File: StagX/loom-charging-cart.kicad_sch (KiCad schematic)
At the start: 0 parts

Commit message: Post comp commit
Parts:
- added BT1: ACCU, symbol Device:Battery
- added Conn: AMPHENOL-21P-Recepticle, symbol Connectors_SUFST:AMPHENOL-21P-Recepticle
- added Conn1, Conn4: Molex_2x1P_Horizontal_THT, symbol Connectors_SUFST:Molex_2x1P_Horizontal_THT
- added Conn5, Conn6: Molex_2x2P_Horizontal, symbol Connectors_SUFST:Molex_2x2P_Horizontal
- added Conn7: AMPHENOL-47P-Recepticle, symbol Connectors_SUFST:AMPHENOL-47P-Recepticle
- added D1: IMD Fault, symbol Device:LED
- added D2: BMS Fault, symbol Device:LED
- added J1: MAINS 16A, symbol Connector_Generic:Conn_01x03
- added J2: CAN_S, symbol Connector:Conn_01x09_Pin
- added K1: Relay_DPST-NO, symbol Relay:Relay_DPST-NO
- added SW1: E-Stop, symbol Switch:SW_Push_Open
- added SW2: Latching Reset, symbol Switch:SW_Push
- added SW3: Close AIRs, symbol Switch:SW_SPST
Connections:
- new net: J1.2 (Pin_2), K1.13
- new net: J1.1 (Pin_1), K1.23
- new net +12V: Conn.3, Conn.5, Conn6.1, Conn7.3, Conn7.5, D1.2 (A), D2.2 (A), K1.A1, SW1.2 (B), SW3.2 (B)
- new net +AIR.AUX.EXC: Conn7.28
- new net +AIR.AUX.GND: Conn7.29
- new net +AIR.INTENDED.ON: Conn7.21
- new net -AIR.AUX.EXC: Conn7.26
- new net -AIR.AUX.GND: Conn7.27
- new net -AIR.INTENDED.ON: Conn7.22
- new net BMS.CHARGE.EXC: Conn.4, Conn7.14
- new net BMS.CHARGER.SAFETY: Conn.9, K1.A2
- new net BMS.EXC: Conn7.4
- new net BMS.FAULT: Conn5.2, Conn7.31
- new net BMS.FAULT.LATCHING: Conn1.2, D2.1 (K)
- new net CAN.CHARGER.HIGH: Conn.11
- new net CAN.CHARGER.LOW: Conn.12
- new net CAN.S.HIGH: Conn.6, Conn7.11, Conn7.9
- new net CAN.S.LOW: Conn.7, Conn7.10, Conn7.12
- new net CHASSIS.GND: Conn7.15
- new net GND: Conn.1, Conn.2, Conn6.2, Conn7.1, Conn7.2
- new net IMD.FAULT.LATCHING: Conn1.1, D1.1 (K)
- new net IMD.OK: Conn5.3, Conn7.16
- new net INV.CLOSE.+AIR: Conn.8, Conn6.4, Conn7.19, Conn7.20
- new net LATCHING.RESET+: Conn4.1, SW2.2
- new net LATCHING.RESET-: Conn4.2, SW2.1
- new net PCHG.AUX.EXC: Conn7.24
- new net PCHG.AUX.GND: Conn7.25
- new net PCHG.INTENDED.ON: Conn7.23
- new net SHUT.LATCHING: Conn6.3, SW1.1 (A)
- new net SHUT.TSAC.INTERLOCK: Conn7.13
- new net TS.ON: Conn7.18, SW3.1 (A)
- new net TS.READY: Conn7.17
- new net TSAC.HVS.EXC: Conn7.6
- new net TSAC.HVS.GND: Conn7.7
- new net ~{BMS.DISCHARGE.ENABLE}: Conn5.1, Conn7.30
- new net ~{TS.DETECTED}: Conn7.8
- no-connect marks 0 -> 11
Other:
- note added: "CAN"
- note added: "CHARGER"
- note added: "Change to socket molex"
- note added: "EARTH"
- note added: "EARTH / CASING"
- note added: "I/O"
- note added: "LATCHING"
- note added: "MAINS"
- note added: "OUTPUT"
- note added: "PANEL"
- note added: "Run over to sidepanel"
- note added: "switch"
- note removed: "Charger Umbilical Separate "shore" power? Charging e-stop loop switches and LED indicators"

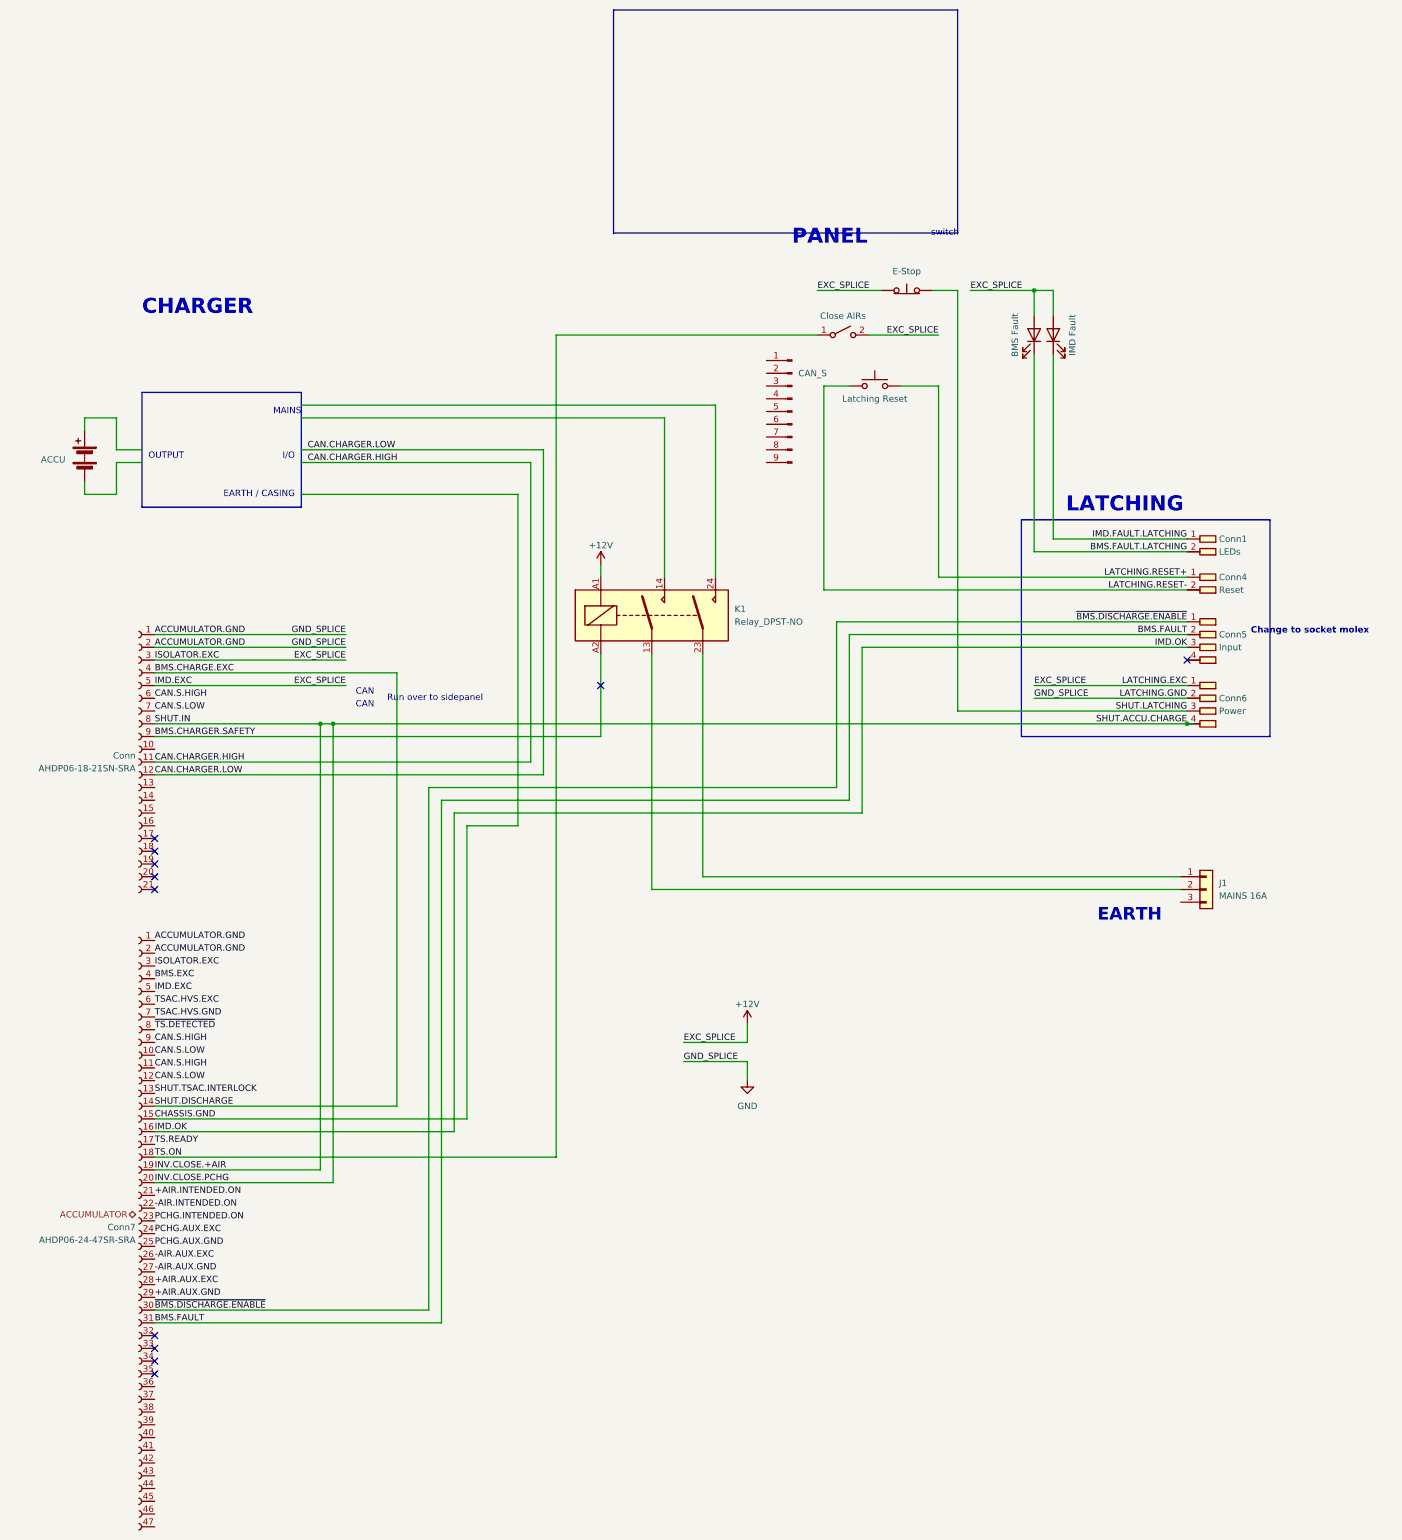
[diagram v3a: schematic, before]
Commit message: Updated charging cart loom to reflect reality, added discharge shut signal to accu loom
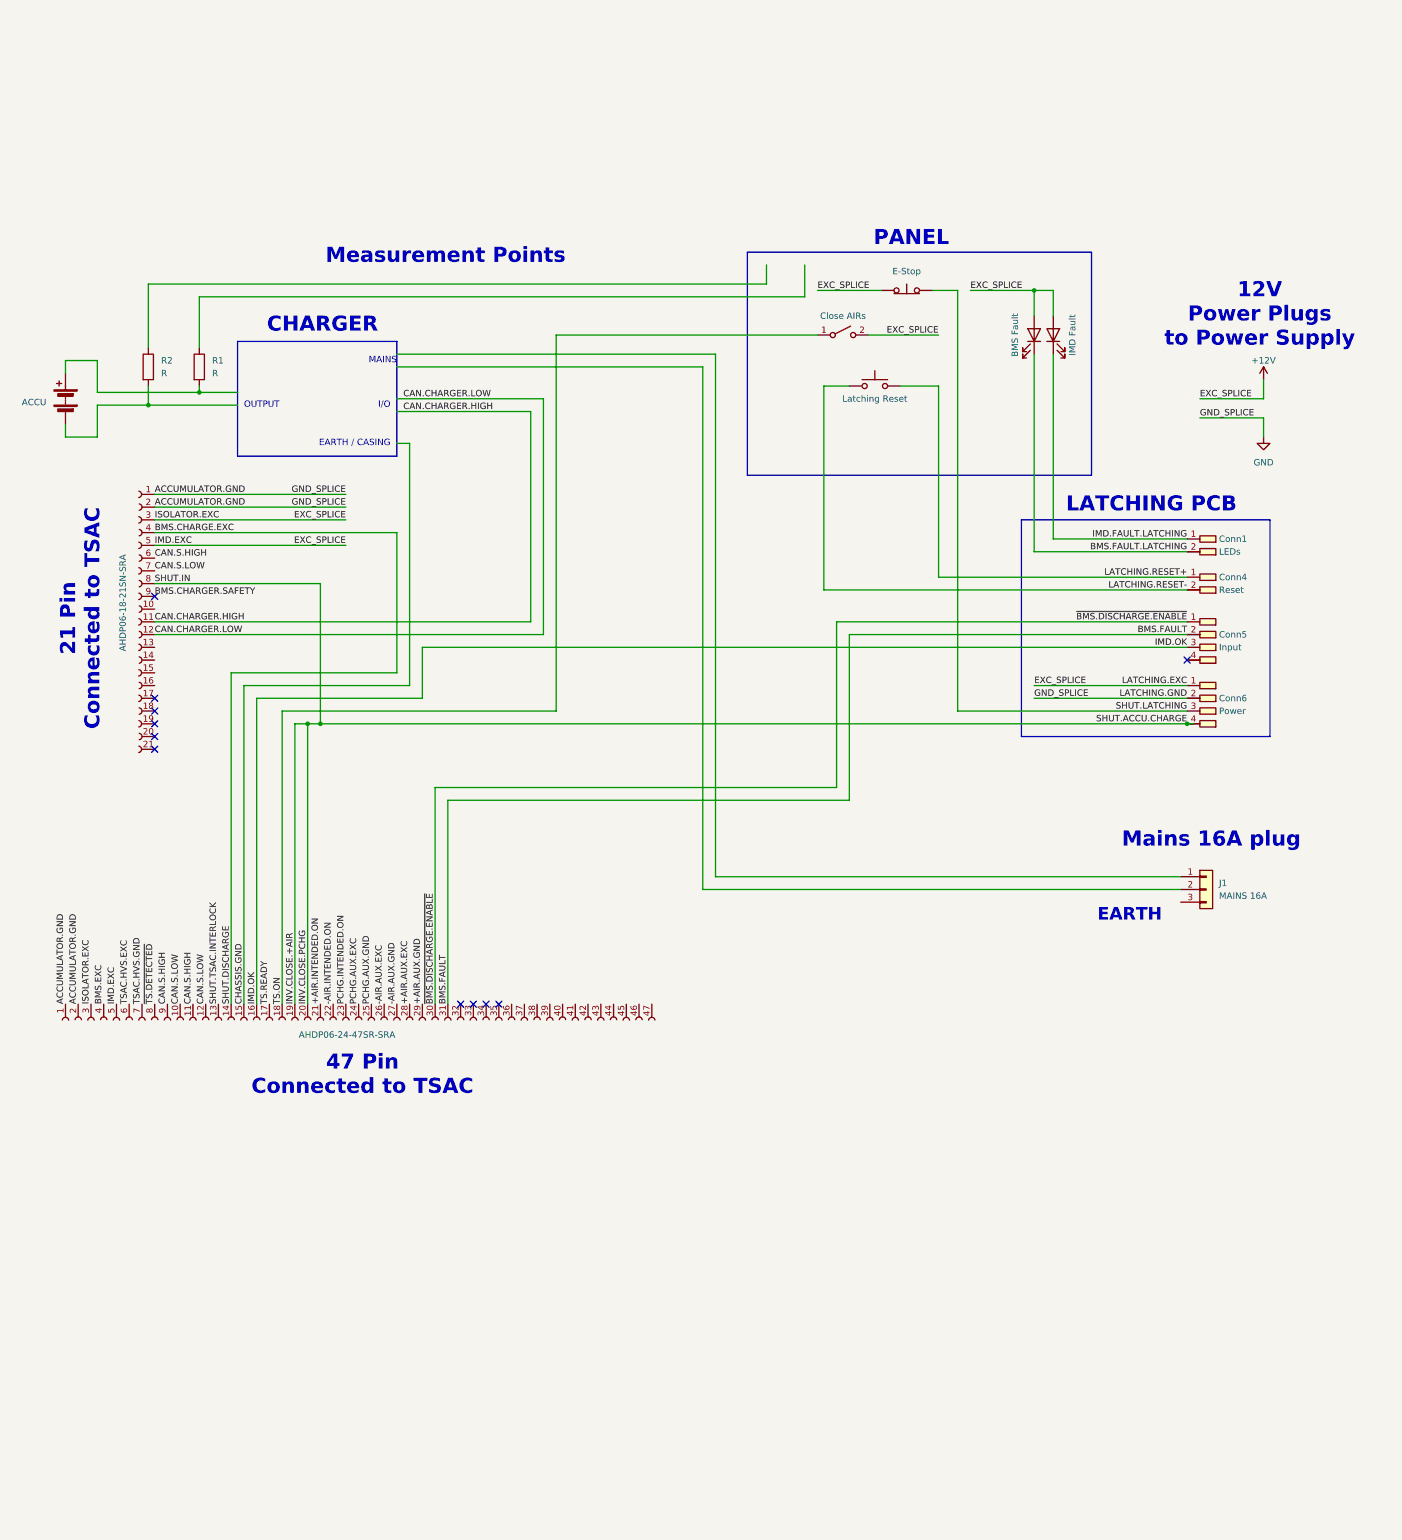
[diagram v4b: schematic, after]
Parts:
- removed J2: CAN_S, symbol Connector:Conn_01x09_Pin
- removed K1: Relay_DPST-NO, symbol Relay:Relay_DPST-NO
- added R1, R2: R, symbol Device:R
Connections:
- net at BT1.1 (+): now also R1.2
- net at BT1.2 (-): now also R2.2
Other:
- note added: "12V Power Plugs to Power Supply"
- note added: "21 Pin Connected to TSAC"
- note added: "47 Pin Connected to TSAC"
- note added: "LATCHING PCB"
- note added: "Mains 16A plug"
- note added: "Measurement Points"
- note removed: "CAN"
- note removed: "Change to socket molex"
- note removed: "LATCHING"
- note removed: "Run over to sidepanel"
- note removed: "switch"
